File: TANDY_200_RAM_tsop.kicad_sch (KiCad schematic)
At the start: 4 parts, among them J1 TANDY_26-3688, U1 62256, U2 74LVC2G00

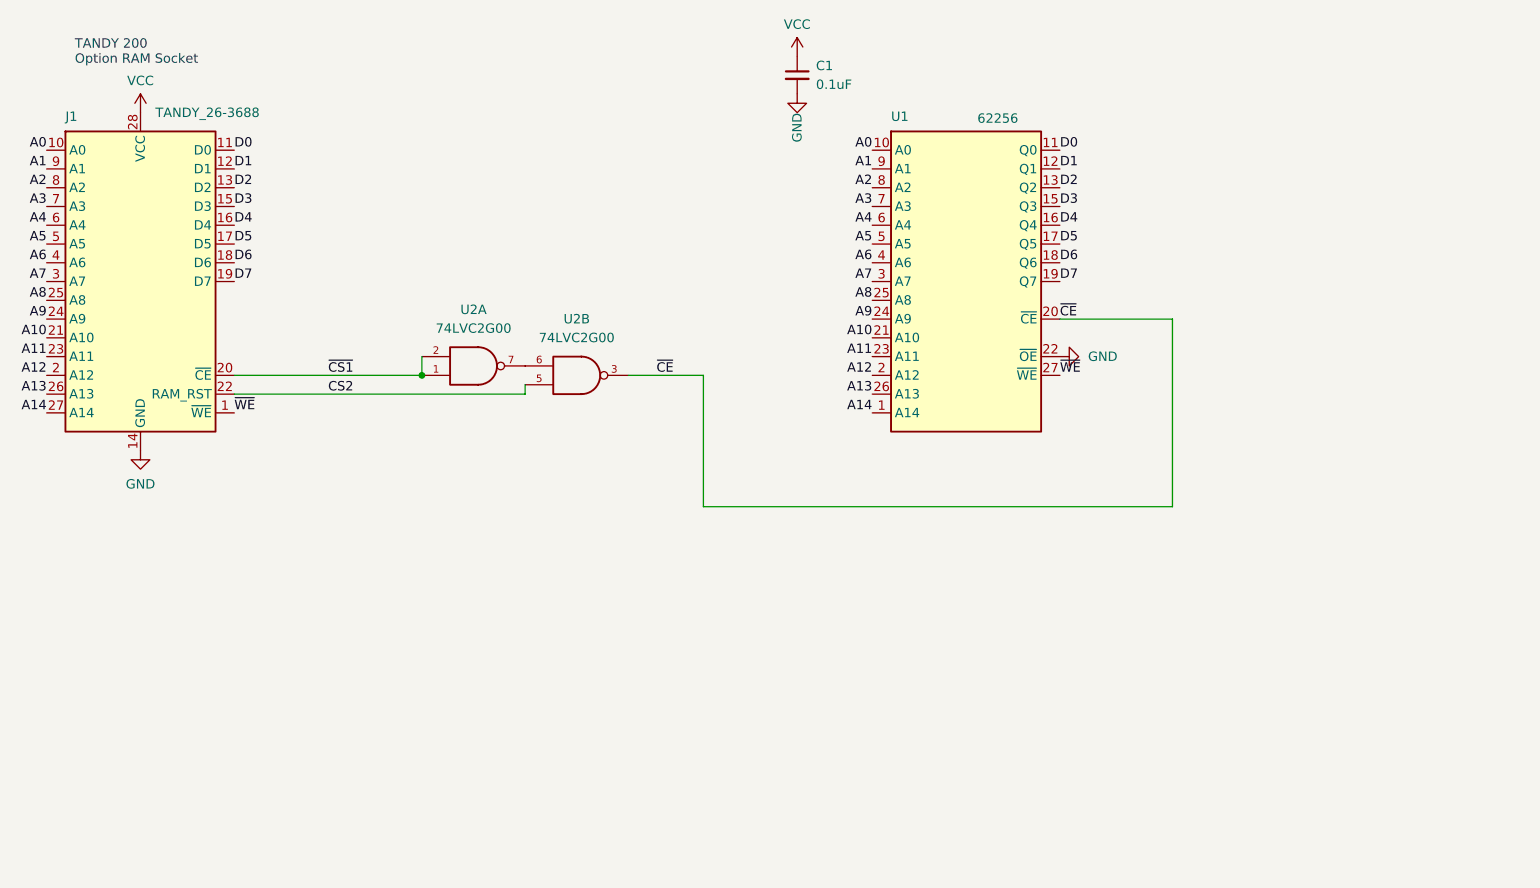
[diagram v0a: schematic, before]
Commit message: ground paths, footprints, sch symbols
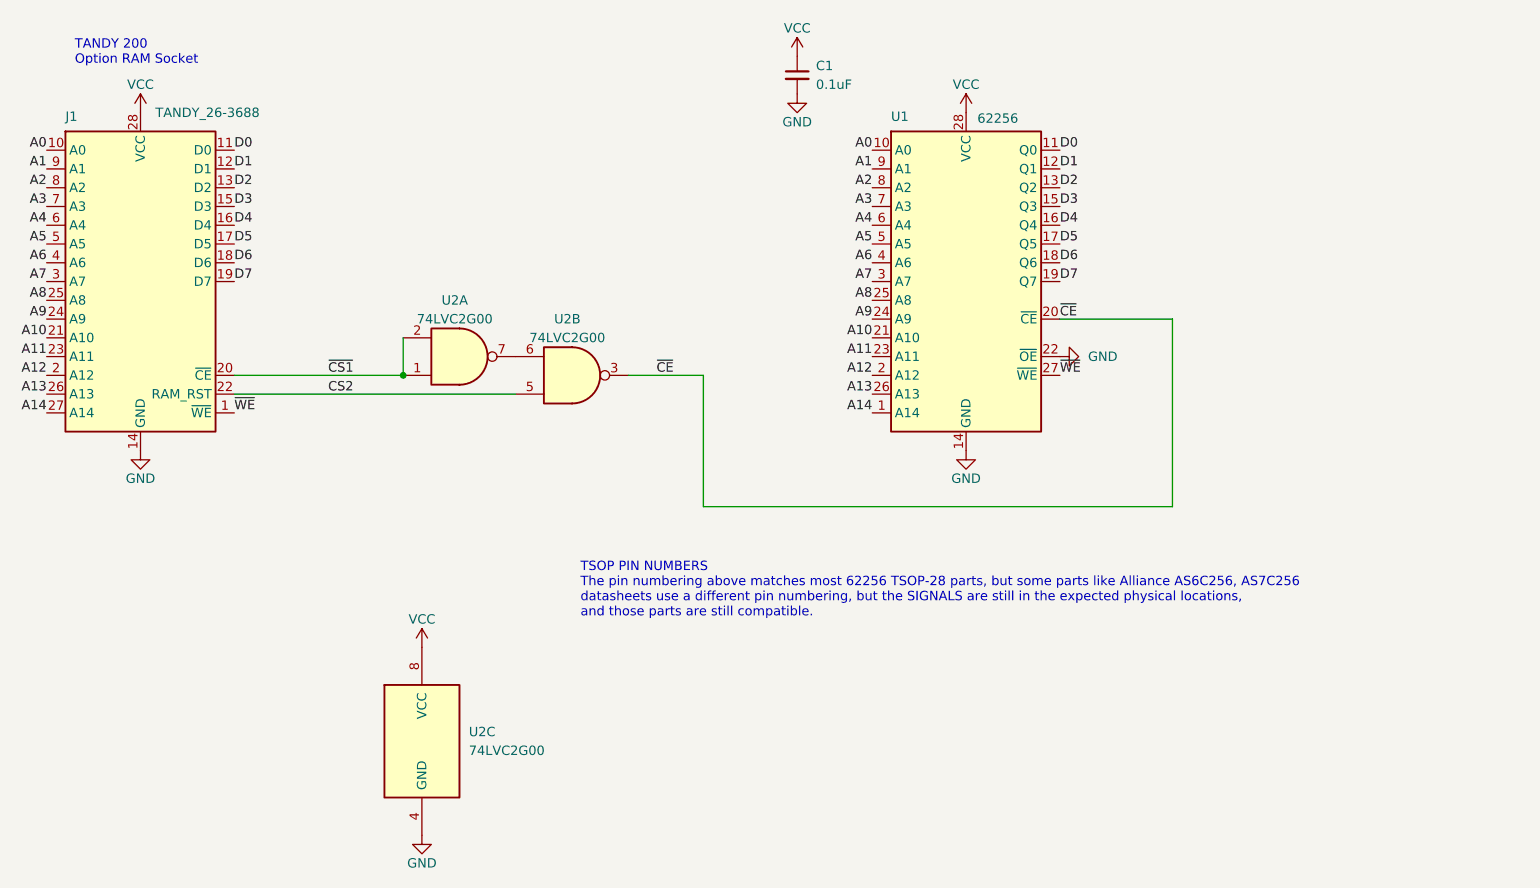
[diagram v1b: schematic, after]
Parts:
- added unit 3 of U2
- U1: footprint 000_LOCAL:TSOP-28-alt -> 000_LOCAL:TSOP-28
- U2: footprint 000_LOCAL:SOT-505-2 -> 000_LOCAL:SSOP-8_2.95x2.8x0.65
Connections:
- net GND: now also U2.4 (GND); no longer U2.4 (GND), U2.4 (GND)
- net VCC: now also U2.8 (VCC); no longer U2.8 (VCC), U2.8 (VCC)
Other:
- note added: "TSOP PIN NUMBERS The pin numbering above matches most 62256 TSOP-28 parts, but some parts like Alliance AS6C256, AS7C256 datasheets use a different pin numbering, but the SIGNALS are still in the expected physical locations, and those parts are still compatible."

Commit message: 24k tsop layout and all board outlines expanded slightly
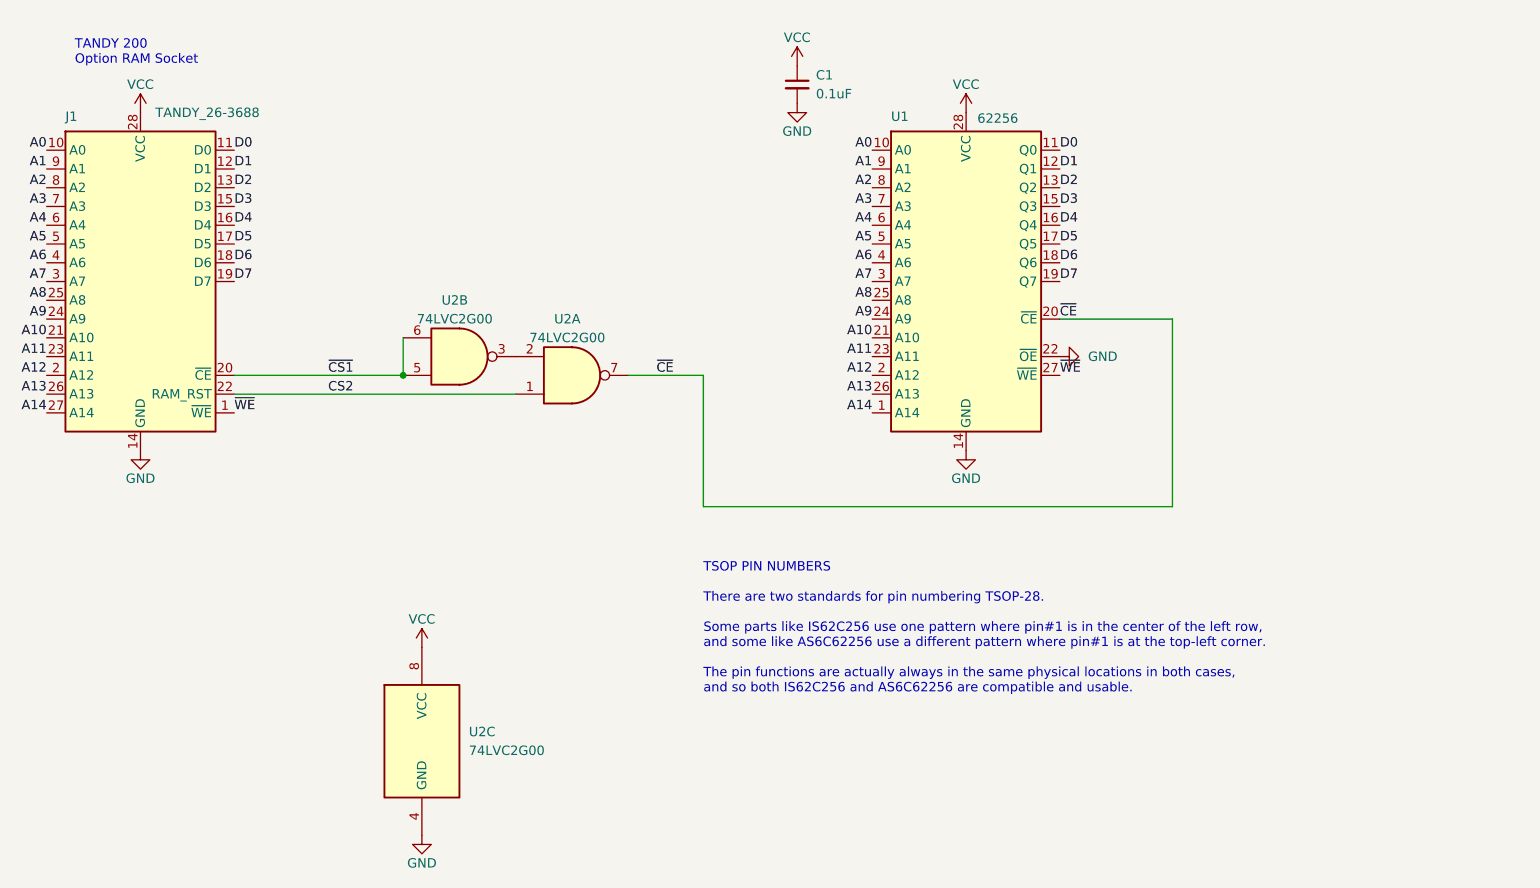
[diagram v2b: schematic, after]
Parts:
- J1: footprint 000_LOCAL:KEL ICC05-028-360TP PCB -> 000_LOCAL:KEL ICC05-028-360TP
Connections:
- net CS2: now also U2.1; no longer U2.5
- net ~{CE}: now also U2.7; no longer U2.3
- net ~{CS1}: now also U2.5, U2.6; no longer U2.1, U2.2
- new net: U2.2, U2.3
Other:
- note added: "TSOP PIN NUMBERS There are two standards for pin numbering TSOP-28. Some parts like IS62C256 use one pattern where pin#1 is in the center of the left row, and some like AS6C62256 use a different pattern where pin#1 is at the top-left corner. The pin functions are actually always in the same physical locations in both cases, and so both IS62C256 and AS6C62256 are compatible and usable."
- note removed: "TSOP PIN NUMBERS The pin numbering above matches most 62256 TSOP-28 parts, but some parts like Alliance AS6C256, AS7C256 datasheets use a different pin numbering, but the SIGNALS are still in the expected physical locations, and those parts are still compatible."
- moved on the sheet: C1, U2A, U2B
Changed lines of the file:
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@@
   (title_block
     (title "TANDY 200 RAM")
-    (date "2022-09-16")
-    (rev "001")
+    (date "2022-10-01")
+    (rev "002")
     (company "b.kenyon.w@gmail.com")
     (comment 1 "github.com/bkw777/TANDY_200_RAM")
@@
     (effects (font (size 1.27 1.27)) (justify left bottom))
   )
-  (text "TSOP PIN NUMBERS\nThe pin numbering above matches most 62256 TSOP-28 parts, but some parts like Alliance AS6C256, AS7C256\ndatasheets use a different pin numbering, but the SIGNALS are still in the expected physical locations,\nand those parts are still compatible.\n"
-    (at 135.763 142.113 0)
+  (text "TSOP PIN NUMBERS\n\nThere are two standards for pin numbering TSOP-28.\n\nSome parts like IS62C256 use one pattern where pin#1 is in the center of the left row,\nand some like AS6C62256 use a different pattern where pin#1 is at the top-left corner.\n\nThe pin functions are actually always in the same physical locations in both cases,\nand so both IS62C256 and AS6C62256 are compatible and usable."
+    (at 152.4 152.4 0)
     (effects (font (size 1.27 1.27)) (justify left bottom))
   )
@@
       (effects (font (size 1.27 1.27)) (justify left))
     )
-    (property "Footprint" "000_LOCAL:KEL ICC05-028-360TP PCB" (id 2) (at 76.2 99.06 0)
+    (property "Footprint" "000_LOCAL:KEL ICC05-028-360TP" (id 2) (at 76.2 99.06 0)
       (effects (font (size 1.27 1.27)) hide)
     )
@@
     (pin "9")
   )
-  (symbol (lib_id "power:VCC") (at 165.1 66.04 0) (unit 1)
-    (in_bom yes) (on_board yes)
-    (property "Reference" "#PWR0106" (id 0) (at 165.1 69.85 0)
-      (effects (font (size 1.27 1.27)) hide)
-    )
-    (property "Value" "VCC" (id 1) (at 165.1 62.23 0))
-    (property "Footprint" "" (id 2) (at 165.1 66.04 0)
-      (effects (font (size 1.27 1.27)) hide)
-    )
-    (property "Datasheet" "" (id 3) (at 165.1 66.04 0)
+  (symbol (lib_id "power:VCC") (at 165.1 67.31 0) (unit 1)
+    (in_bom yes) (on_board yes)
+    (property "Reference" "#PWR0106" (id 0) (at 165.1 71.12 0)
+      (effects (font (size 1.27 1.27)) hide)
+    )
+    (property "Value" "VCC" (id 1) (at 165.1 63.5 0))
+    (property "Footprint" "" (id 2) (at 165.1 67.31 0)
+      (effects (font (size 1.27 1.27)) hide)
+    )
+    (property "Datasheet" "" (id 3) (at 165.1 67.31 0)
       (effects (font (size 1.27 1.27)) hide)
     )
@@
     (pin "1")
   )
-  (symbol (lib_id "power:GND") (at 165.1 71.12 0) (unit 1)
-    (in_bom yes) (on_board yes)
-    (property "Reference" "#PWR0105" (id 0) (at 165.1 77.47 0)
-      (effects (font (size 1.27 1.27)) hide)
-    )
-    (property "Value" "GND" (id 1) (at 165.1 74.93 0))
-    (property "Footprint" "" (id 2) (at 165.1 71.12 0)
-      (effects (font (size 1.27 1.27)) hide)
-    )
-    (property "Datasheet" "" (id 3) (at 165.1 71.12 0)
-      (effects (font (size 1.27 1.27)) hide)
-    )
-    (pin "1")
-  )
-  (symbol (lib_id "000_LOCAL:C") (at 165.1 68.58 0) (unit 1)
+  (symbol (lib_id "power:GND") (at 165.1 72.39 0) (unit 1)
+    (in_bom yes) (on_board yes)
+    (property "Reference" "#PWR0105" (id 0) (at 165.1 78.74 0)
+      (effects (font (size 1.27 1.27)) hide)
+    )
+    (property "Value" "GND" (id 1) (at 165.1 76.2 0))
+    (property "Footprint" "" (id 2) (at 165.1 72.39 0)
+      (effects (font (size 1.27 1.27)) hide)
+    )
+    (property "Datasheet" "" (id 3) (at 165.1 72.39 0)
+      (effects (font (size 1.27 1.27)) hide)
+    )
+    (pin "1")
+  )
+  (symbol (lib_id "000_LOCAL:C") (at 165.1 69.85 0) (unit 1)
     (in_bom yes) (on_board yes) (fields_autoplaced)
-    (property "Reference" "C1" (id 0) (at 167.64 67.3162 0)
+    (property "Reference" "C1" (id 0) (at 167.64 68.5862 0)
       (effects (font (size 1.27 1.27)) (justify left))
     )
-    (property "Value" "0.1uF" (id 1) (at 167.64 69.8562 0)
+    (property "Value" "0.1uF" (id 1) (at 167.64 71.1262 0)
       (effects (font (size 1.27 1.27)) (justify left))
     )
-    (property "Footprint" "000_LOCAL:C_0805" (id 2) (at 165.1 68.58 0)
-      (effects (font (size 1.27 1.27)) hide)
-    )
-    (property "Datasheet" "~" (id 3) (at 165.1 68.58 0)
+    (property "Footprint" "000_LOCAL:C_0805" (id 2) (at 165.1 69.85 0)
+      (effects (font (size 1.27 1.27)) hide)
+    )
+    (property "Datasheet" "~" (id 3) (at 165.1 69.85 0)
       (effects (font (size 1.27 1.27)) hide)
     )
@@
     (pin "2")
   )
-  (symbol (lib_id "000_LOCAL:74LVC2G00") (at 134.62 109.22 0) (mirror x) (unit 2)
+  (symbol (lib_id "000_LOCAL:74LVC2G00") (at 119.38 106.68 0) (mirror x) (unit 2)
     (in_bom yes) (on_board yes) (fields_autoplaced)
-    (property "Reference" "U2" (id 0) (at 133.985 101.6 0))
-    (property "Value" "74LVC2G00" (id 1) (at 133.985 104.14 0))
-    (property "Footprint" "000_LOCAL:SSOP-8_2.95x2.8x0.65" (id 2) (at 134.62 109.22 0)
-      (effects (font (size 1.27 1.27)) hide)
-    )
-    (property "Datasheet" "https://www.ti.com/lit/gpn/sn74lvc2g00" (id 3) (at 134.62 109.22 0)
+    (property "Reference" "U2" (id 0) (at 118.745 99.06 0))
+    (property "Value" "74LVC2G00" (id 1) (at 118.745 101.6 0))
+    (property "Footprint" "000_LOCAL:SSOP-8_2.95x2.8x0.65" (id 2) (at 119.38 106.68 0)
+      (effects (font (size 1.27 1.27)) hide)
+    )
+    (property "Datasheet" "https://www.ti.com/lit/gpn/sn74lvc2g00" (id 3) (at 119.38 106.68 0)
       (effects (font (size 1.27 1.27)) hide)
     )
@@
     (pin "1")
   )
-  (symbol (lib_name "74LVC2G00_1") (lib_id "000_LOCAL:74LVC2G00") (at 119.38 106.68 0) (mirror x) (unit 1)
+  (symbol (lib_name "74LVC2G00_1") (lib_id "000_LOCAL:74LVC2G00") (at 134.62 109.22 0) (mirror x) (unit 1)
     (in_bom yes) (on_board yes) (fields_autoplaced)
-    (property "Reference" "U2" (id 0) (at 118.745 99.06 0))
-    (property "Value" "74LVC2G00" (id 1) (at 118.745 101.6 0))
-    (property "Footprint" "000_LOCAL:SSOP-8_2.95x2.8x0.65" (id 2) (at 119.38 106.68 0)
-      (effects (font (size 1.27 1.27)) hide)
-    )
-    (property "Datasheet" "https://www.ti.com/lit/gpn/sn74lvc2g00" (id 3) (at 119.38 106.68 0)
+    (property "Reference" "U2" (id 0) (at 133.985 101.6 0))
+    (property "Value" "74LVC2G00" (id 1) (at 133.985 104.14 0))
+    (property "Footprint" "000_LOCAL:SSOP-8_2.95x2.8x0.65" (id 2) (at 134.62 109.22 0)
+      (effects (font (size 1.27 1.27)) hide)
+    )
+    (property "Datasheet" "https://www.ti.com/lit/gpn/sn74lvc2g00" (id 3) (at 134.62 109.22 0)
       (effects (font (size 1.27 1.27)) hide)
     )
@@
     )
     (path "/0ca43401-3dca-436a-b184-791083c316bb"
-      (reference "J1") (unit 1) (value "TANDY_26-3688") (footprint "000_LOCAL:KEL ICC05-028-360TP PCB")
+      (reference "J1") (unit 1) (value "TANDY_26-3688") (footprint "000_LOCAL:KEL ICC05-028-360TP")
     )
     (path "/c63808ae-1f01-41cd-bf76-9618093de932"
